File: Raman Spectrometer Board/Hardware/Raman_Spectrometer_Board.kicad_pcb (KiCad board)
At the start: 2 copper layers, 105.4 x 36.8 mm, 21 parts, among them J1 RJ45_LED_Shielded, Q1 BSS138, Q2 BSS138, U1 Teensy4.1_DEV-16771, U2 OKI

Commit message: //WIP
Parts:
- C2: moved to B.Cu
- moved C3 26.0 mm to (114.3, 46.7), turned to -90 degrees
- moved U2 15.1 mm to (109.2, 43.8), turned to 0 degrees
- moved R1 14.6 mm to (98.0, 51.8), turned to -90 degrees
- moved C2 12.3 mm to (111.8, 46.6)
- moved R2 5.70 mm to (98.0, 47.8), turned to -90 degrees
- moved Q2 1.01 mm to (102.2, 46.2), turned to 90 degrees
- moved Q1 0.88 mm to (102.2, 53.3), turned to 90 degrees
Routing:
- net +12V: track 0.00 -> 103.8 mm
- net +5V: track 0.00 -> 76.9 mm
- net +3V3: track 0.00 -> 52.0 mm
- net Red_LED: track 0.00 -> 4.98 mm
- net Green_LED: track 0.00 -> 4.98 mm
- net CCD_ROG_5V: track 0.00 -> 4.14 mm, vias 0 -> 1
- net Net-(D2-K): track 0.00 -> 2.39 mm
- net Net-(D3-K): track 0.00 -> 2.38 mm
- net Net-(D1-K): track 0.00 -> 2.38 mm
- net CCD_CLK_5V: track 0.00 -> 1.99 mm, vias 0 -> 1
- net GND: track 0.00 -> 1.91 mm

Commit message: feat: finish Raman board
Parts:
- C1: moved to B.Cu
- moved C1 16.1 mm to (43.2, 38.9), turned to 180 degrees
- moved R1 7.08 mm to (105.1, 52.8)
- moved R2 7.08 mm to (105.1, 48.8)
- moved Q1 3.19 mm to (99.4, 54.9)
- moved Q2 3.19 mm to (99.4, 47.8)
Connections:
- U1 pad 24: CCD_CLK_3V3 -> CCD_ROG_3V3
- U1 pad 25: CCD_ROG_3V3 -> CCD_CLK_3V3
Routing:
- net +3V3: track 52.0 -> 112.4 mm
- net LED: track 0.00 -> 37.0 mm
- net +5V: track 76.9 -> 106.9 mm, vias 0 -> 1
- net R-: track 0.00 -> 29.4 mm, vias 0 -> 1
- net R+: track 0.00 -> 29.2 mm, vias 0 -> 1
- net T+: track 0.00 -> 28.4 mm
- net T-: track 0.00 -> 28.3 mm
- net CCD_CLK_5V: track 1.99 -> 25.2 mm
- net CCD_Vout: track 0.00 -> 20.5 mm
- net CCD_ROG_5V: track 4.14 -> 23.5 mm
- net CCD_CLK_3V3: track 0.00 -> 17.3 mm
- net Net-(C1-Pad1): track 0.00 -> 14.2 mm
- net CCD_ROG_3V3: track 0.00 -> 9.09 mm

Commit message: fix: changes from malacki
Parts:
- moved R3 5.80 mm to (52.1, 49.8), turned to 180 degrees
- moved R4 5.80 mm to (52.1, 53.6), turned to 180 degrees
- moved R5 5.69 mm to (52.2, 56.9), turned to 180 degrees
- moved D3 2.66 mm to (56.4, 56.9), turned to 0 degrees
- moved D1 2.56 mm to (56.3, 49.8), turned to 0 degrees
- moved D2 2.55 mm to (56.3, 53.6), turned to 0 degrees
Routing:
- net +3V3: track 112.4 -> 104.8 mm
- net +5V: track 106.9 -> 102.4 mm
- net +12V: track 103.8 -> 99.5 mm
- net GND: vias 0 -> 6

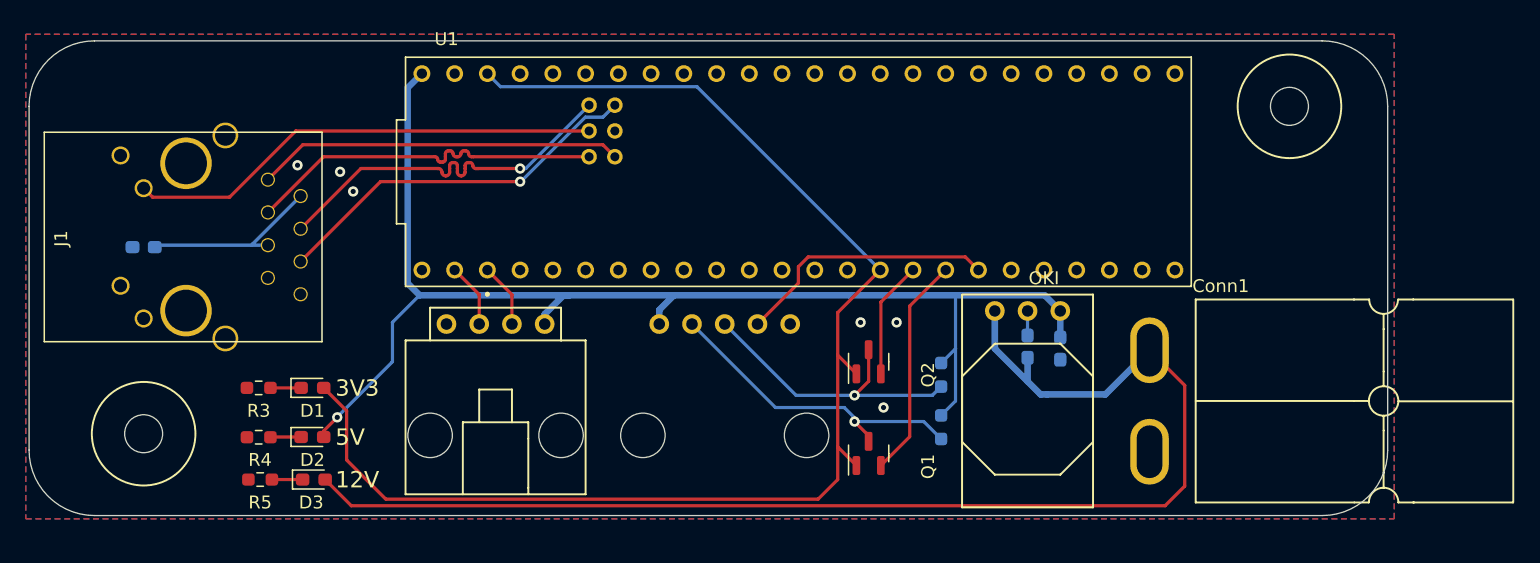
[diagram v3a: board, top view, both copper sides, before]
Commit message: switched raman board to using vertical molex
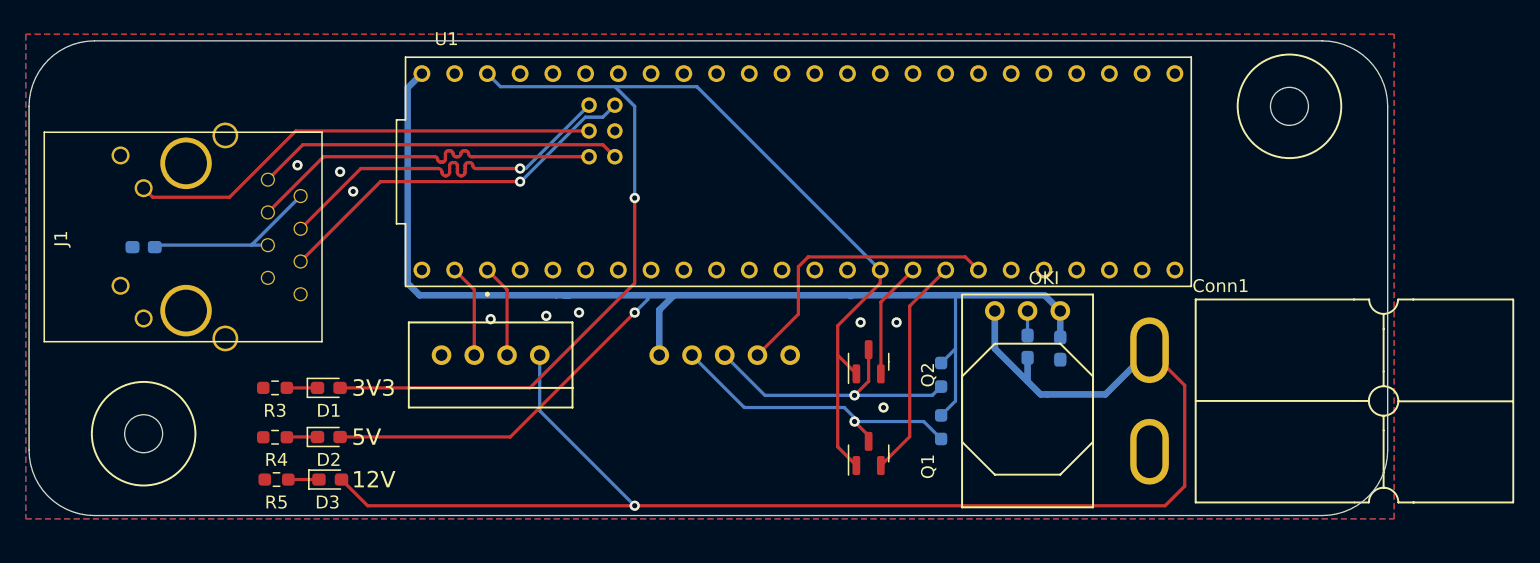
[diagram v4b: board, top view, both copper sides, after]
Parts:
- Conn2: footprint MRDT_Connectors:MOLEX_SL_05_Horizontal -> MRDT_Connectors:MOLEX_SL_05_Vertical
- Conn3: footprint MRDT_Connectors:MOLEX_SL_04_Horizontal -> MRDT_Connectors:MOLEX_SL_04_Vertical
- moved Conn3 2.44 mm to (73.9, 47.2)
- moved Conn2 2.41 mm to (83.2, 47.2)
- moved D1 1.27 mm to (57.5, 49.8)
- moved D2 1.27 mm to (57.5, 53.6)
- moved D3 1.27 mm to (57.7, 56.9)
- moved R3 1.27 mm to (53.4, 49.8)
- moved R4 1.27 mm to (53.4, 53.6)
- moved R5 1.27 mm to (53.5, 56.9)
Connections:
- Conn3 pad 1: +5V -> +12V
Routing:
- net +5V: track 102.4 -> 116.1 mm
- net +12V: track 99.5 -> 112.9 mm, vias 0 -> 1
- net +3V3: track 104.8 -> 98.1 mm, vias 0 -> 1
- net CCD_Vout: track 20.5 -> 22.9 mm
- net Red_LED: track 4.98 -> 7.24 mm
- net Green_LED: track 4.98 -> 7.24 mm
- net CCD_ROG_5V: track 23.5 -> 22.5 mm
- net CCD_CLK_5V: track 25.2 -> 24.2 mm
- net GND: vias 6 -> 9

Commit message: rearrange components on raman board
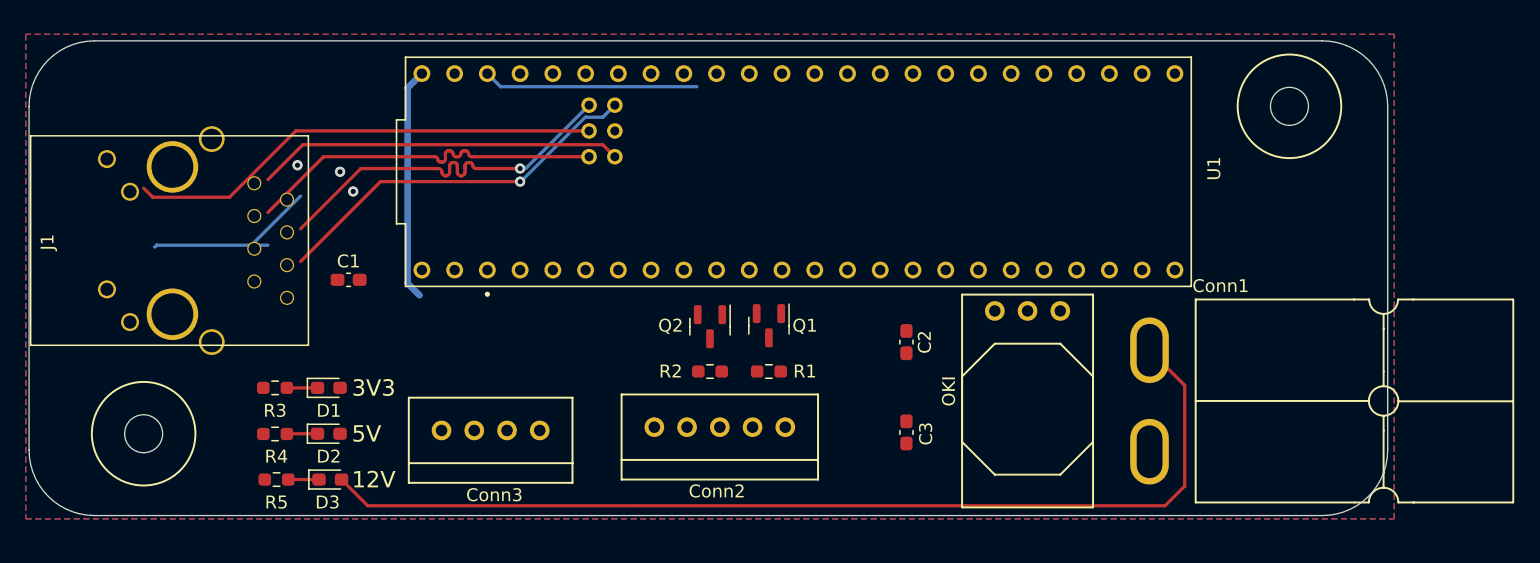
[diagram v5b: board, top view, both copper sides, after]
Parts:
- C1, C2, C3, Conn2, R1, R2: moved to F.Cu
- moved R2 17.9 mm to (87.1, 48.5), turned to 0 degrees
- moved C1 16.1 mm to (59.1, 41.4), turned to 0 degrees
- moved R1 14.0 mm to (91.7, 48.5), turned to 180 degrees
- moved C3 13.6 mm to (102.4, 53.2), turned to 90 degrees
- moved Q2 12.6 mm to (87.1, 45.0), turned to -90 degrees
- moved Q1 12.6 mm to (91.7, 45.0), turned to -90 degrees
- moved Conn2 11.3 mm to (93.0, 52.8), turned to 180 degrees
- moved C2 9.40 mm to (102.4, 46.2), turned to -90 degrees
- moved Conn3 5.84 mm to (73.9, 53.1)
- moved J1 1.09 mm to (32.4, 38.5)
- moved D2 0.25 mm to (57.5, 53.3)
- moved R4 0.25 mm to (53.4, 53.4)
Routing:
- net +5V: track 116.1 -> 18.0 mm, vias 1 -> 0
- net +3V3: track 98.1 -> 16.7 mm, vias 1 -> 0
- net +12V: track 112.9 -> 78.6 mm, vias 1 -> 0
- net CCD_CLK_5V: track 24.2 -> 0.00 mm, vias 1 -> 0
- net CCD_Vout: track 22.9 -> 0.00 mm
- net CCD_ROG_5V: track 22.5 -> 0.00 mm, vias 1 -> 0
- net CCD_CLK_3V3: track 17.3 -> 0.00 mm
- net CCD_ROG_3V3: track 9.09 -> 0.00 mm
- net Red_LED: track 7.24 -> 0.00 mm
- net Green_LED: track 7.24 -> 0.00 mm
- net GND: track 1.91 -> 0.00 mm, vias 9 -> 3

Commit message: added signatures to all boards
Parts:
- added G***: LOGO, Signatures:Caleb_Ehlers_Signature_15mmx4.8mm, F.Cu at (43.2, 25.9)

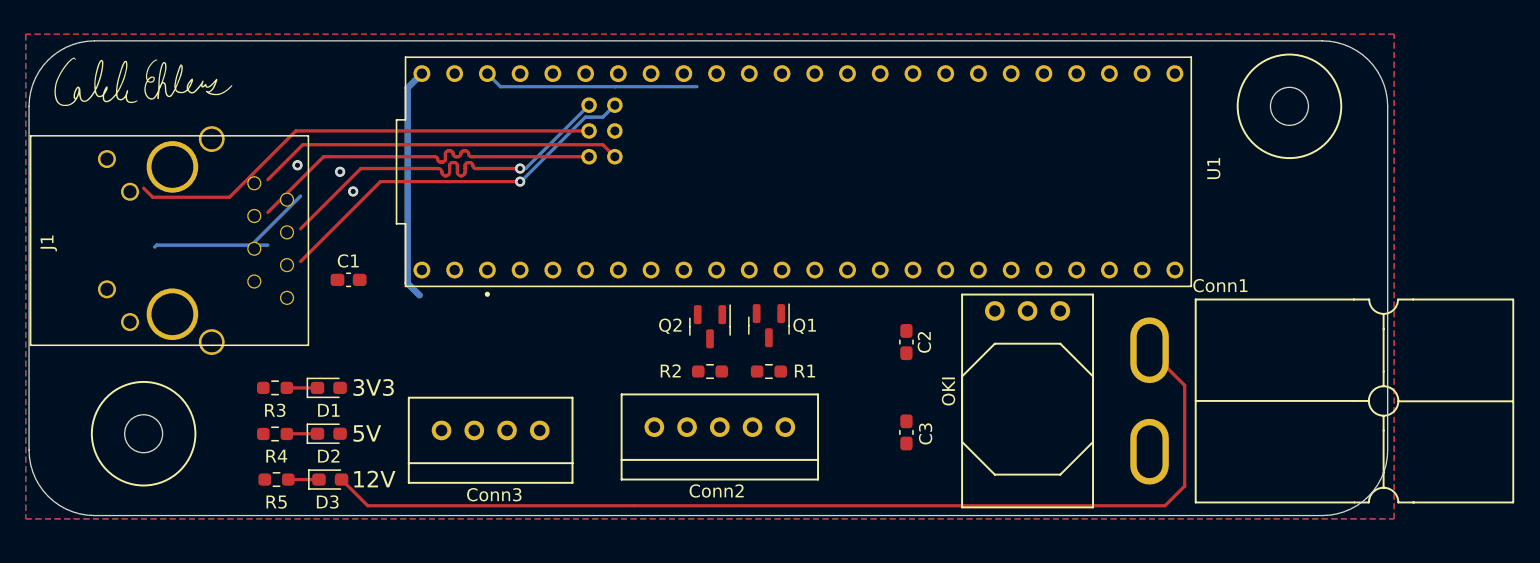
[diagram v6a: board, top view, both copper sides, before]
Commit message: rewired raman board
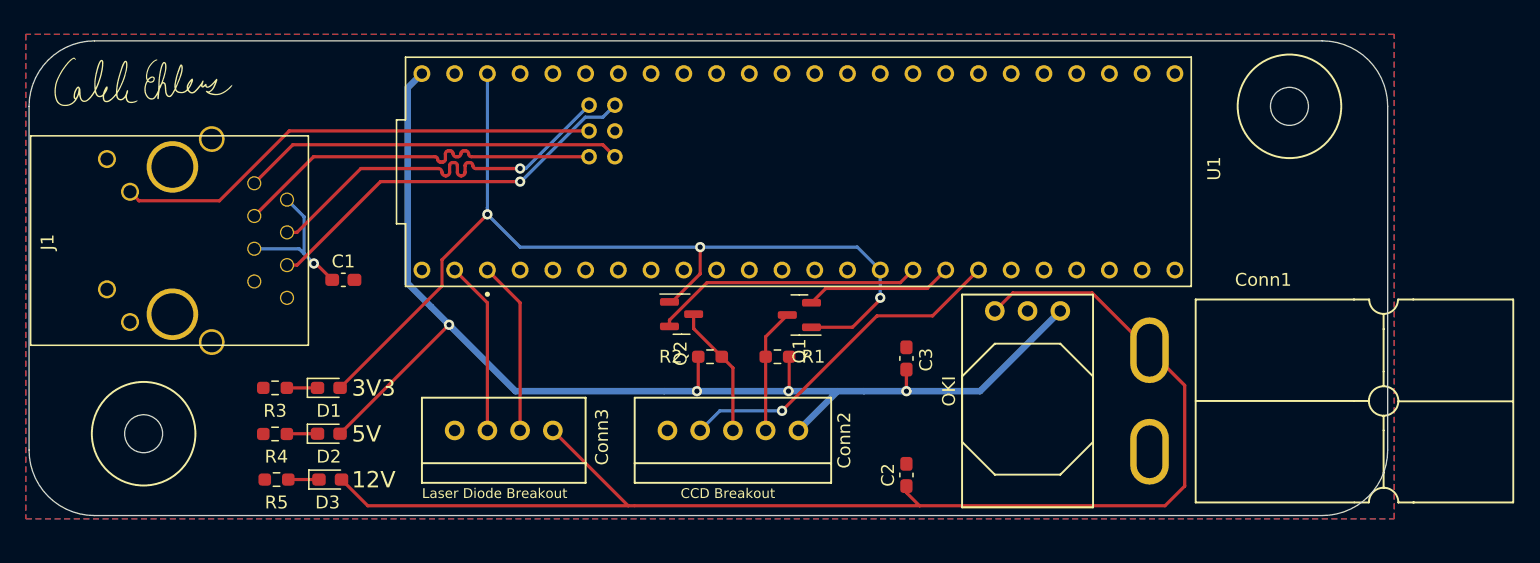
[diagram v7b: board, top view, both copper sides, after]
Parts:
- moved C2 10.3 mm to (102.4, 56.5), turned to 90 degrees
- moved C3 5.74 mm to (102.4, 47.5)
- moved Q1 2.51 mm to (94.1, 44.1), turned to 180 degrees
- moved Q2 2.41 mm to (84.9, 44.1), turned to 0 degrees
- moved R1 1.32 mm to (92.4, 47.4)
- moved R2 1.15 mm to (87.1, 47.4)
- moved Conn2 1.05 mm to (94.0, 53.1)
- moved Conn3 1.02 mm to (74.9, 53.1)
- moved C1 0.41 mm to (58.7, 41.4)
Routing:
- net +5V: track 18.0 -> 96.8 mm, vias 0 -> 4
- net +3V3: track 16.7 -> 75.3 mm, vias 0 -> 3
- net CCD_Vout: track 0.00 -> 26.7 mm, vias 0 -> 1
- net +12V: track 78.6 -> 103.2 mm
- net CCD_ROG_3V3: track 0.00 -> 21.0 mm
- net Red_LED: track 0.00 -> 13.5 mm
- net Green_LED: track 0.00 -> 13.5 mm
- net CCD_CLK_3V3: track 0.00 -> 11.5 mm
- net CCD_ROG_5V: track 0.00 -> 10.3 mm
- net CCD_CLK_5V: track 0.00 -> 9.65 mm
- net Net-(C1-Pad1): track 14.2 -> 11.9 mm, vias 0 -> 1
- net R-: track 29.4 -> 30.6 mm
- net R+: track 29.2 -> 30.4 mm
- net T-: track 28.3 -> 29.5 mm
- net T+: track 28.4 -> 29.6 mm
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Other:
- board text added: "CCD Breakout"
- board text added: "Laser Diode Breakout"

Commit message: clean up 3V3 wires
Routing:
- net +3V3: track 75.3 -> 106.8 mm
- net GND: vias 0 -> 7
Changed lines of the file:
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@@
   (segment (start 56.388 40.132) (end 56.5415 40.132) (width 0.25) (layer "F.Cu") (net 1))
   (via (at 56.388 40.132) (size 0.8) (drill 0.4) (layers "F.Cu" "B.Cu") (net 1))
-  (segment (start 55.626 39.37) (end 55.626 36.5005) (width 0.25) (layer "B.Cu") (net 1))
   (segment (start 55.626 36.5005) (end 54.3045 35.179) (width 0.25) (layer "B.Cu") (net 1))
   (segment (start 51.652 38.608) (end 51.652 38.62) (width 0.254) (layer "B.Cu") (net 1))
+  (segment (start 55.626 39.37) (end 55.626 36.5005) (width 0.25) (layer "B.Cu") (net 1))
   (segment (start 56.388 40.132) (end 55.626 39.37) (width 0.25) (layer "B.Cu") (net 1))
   (segment (start 51.652 38.62) (end 51.562 38.71) (width 0.254) (layer "B.Cu") (net 1))
@@
   (segment (start 55.245 38.989) (end 51.7645 38.989) (width 0.25) (layer "B.Cu") (net 1))
   (segment (start 102.362 46.6355) (end 102.362 46.736) (width 0.25) (layer "F.Cu") (net 2))
+  (via (at 101.346 42.926) (size 0.8) (drill 0.4) (layers "F.Cu" "B.Cu") (free) (net 2))
+  (via (at 71.12 43.688) (size 0.8) (drill 0.4) (layers "F.Cu" "B.Cu") (free) (net 2))
+  (via (at 88.392 45.466) (size 0.8) (drill 0.4) (layers "F.Cu" "B.Cu") (free) (net 2))
+  (via (at 90.17 44.196) (size 0.8) (drill 0.4) (layers "F.Cu" "B.Cu") (free) (net 2))
+  (via (at 71.12 51.308) (size 0.8) (drill 0.4) (layers "F.Cu" "B.Cu") (free) (net 2))
+  (via (at 97.282 43.942) (size 0.8) (drill 0.4) (layers "F.Cu" "B.Cu") (free) (net 2))
+  (via (at 88.392 43.18) (size 0.8) (drill 0.4) (layers "F.Cu" "B.Cu") (free) (net 2))
   (segment (start 109.22 43.815) (end 110.617 42.418) (width 0.25) (layer "F.Cu") (net 3))
   (segment (start 60.565 58.928) (end 80.772 58.928) (width 0.254) (layer "F.Cu") (net 3))
@@
   (segment (start 86.887749 41.619) (end 83.983498 44.523251) (width 0.25) (layer "F.Cu") (net 20))
   (segment (start 83.983498 44.523251) (end 83.977 44.523251) (width 0.25) (layer "F.Cu") (net 20))
-  (segment (start 86.36 40.931) (end 84.177 43.114) (width 0.25) (layer "F.Cu") (net 53))
-  (segment (start 66.331 41.873) (end 66.331 39.841) (width 0.25) (layer "F.Cu") (net 53))
-  (segment (start 100.33 42.7935) (end 100.33 42.926) (width 0.25) (layer "F.Cu") (net 53))
-  (segment (start 98.176 45.08) (end 94.996 45.08) (width 0.25) (layer "F.Cu") (net 53))
-  (segment (start 66.331 39.841) (end 69.85 36.322) (width 0.25) (layer "F.Cu") (net 53))
+  (segment (start 94.996 48.015622) (end 93.989622 49.022) (width 0.25) (layer "F.Cu") (net 53))
+  (segment (start 83.977 43.114) (end 82.55 44.541) (width 0.25) (layer "F.Cu") (net 53))
+  (segment (start 58.42 49.784) (end 59.69 49.784) (width 0.25) (layer "F.Cu") (net 53))
   (segment (start 84.177 43.114) (end 83.977 43.114) (width 0.25) (layer "F.Cu") (net 53))
-  (segment (start 86.36 38.862) (end 86.36 40.931) (width 0.25) (layer "F.Cu") (net 53))
-  (segment (start 58.42 49.784) (end 66.331 41.873) (width 0.25) (layer "F.Cu") (net 53))
-  (segment (start 100.33 42.926) (end 98.176 45.08) (width 0.25) (layer "F.Cu") (net 53))
-  (via (at 86.36 38.862) (size 0.8) (drill 0.4) (layers "F.Cu" "B.Cu") (net 53))
-  (via (at 69.85 36.322) (size 0.8) (drill 0.4) (layers "F.Cu" "B.Cu") (net 53))
-  (via (at 100.33 42.7935) (size 0.8) (drill 0.4) (layers "F.Cu" "B.Cu") (net 53))
-  (segment (start 98.552 38.862) (end 100.33 40.64) (width 0.25) (layer "B.Cu") (net 53))
-  (segment (start 86.36 38.862) (end 98.552 38.862) (width 0.25) (layer "B.Cu") (net 53))
-  (segment (start 69.85 36.322) (end 69.85 35.814) (width 0.25) (layer "B.Cu") (net 53))
-  (segment (start 86.36 38.862) (end 72.39 38.862) (width 0.25) (layer "B.Cu") (net 53))
-  (segment (start 69.85 25.4) (end 69.85 35.814) (width 0.25) (layer "B.Cu") (net 53))
-  (segment (start 100.33 42.7935) (end 100.33 40.64) (width 0.25) (layer "B.Cu") (net 53))
-  (segment (start 72.39 38.862) (end 69.85 36.322) (width 0.25) (layer "B.Cu") (net 53))
+  (segment (start 59.69 49.784) (end 66.548 42.926) (width 0.25) (layer "F.Cu") (net 53))
+  (segment (start 82.55 44.541) (end 82.55 49.022) (width 0.25) (layer "F.Cu") (net 53))
+  (segment (start 94.996 45.08) (end 94.996 48.015622) (width 0.25) (layer "F.Cu") (net 53))
+  (via (at 66.548 42.926) (size 0.8) (drill 0.4) (layers "F.Cu" "B.Cu") (net 53))
+  (via (at 82.55 49.022) (size 0.8) (drill 0.4) (layers "F.Cu" "B.Cu") (net 53))
+  (via (at 93.989622 49.022) (size 0.8) (drill 0.4) (layers "F.Cu" "B.Cu") (net 53))
+  (segment (start 66.04 29.21) (end 66.04 39.878) (width 0.25) (layer "B.Cu") (net 53))
+  (segment (start 72.644 49.022) (end 93.989622 49.022) (width 0.25) (layer "B.Cu") (net 53))
+  (segment (start 69.85 25.4) (end 66.04 29.21) (width 0.25) (layer "B.Cu") (net 53))
+  (segment (start 66.04 42.418) (end 72.644 49.022) (width 0.25) (layer "B.Cu") (net 53))
+  (segment (start 98.552 38.862) (end 67.056 38.862) (width 0.25) (layer "B.Cu") (net 53))
+  (segment (start 67.056 38.862) (end 66.04 39.878) (width 0.25) (layer "B.Cu") (net 53))
+  (segment (start 100.33 40.64) (end 98.552 38.862) (width 0.25) (layer "B.Cu") (net 53))
+  (segment (start 66.04 39.878) (end 66.04 42.418) (width 0.25) (layer "B.Cu") (net 53))
   (segment (start 54.31 53.34) (end 54.29 53.36) (width 0.25) (layer "F.Cu") (net 54))
   (segment (start 56.67 53.34) (end 54.31 53.34) (width 0.25) (layer "F.Cu") (net 54))
